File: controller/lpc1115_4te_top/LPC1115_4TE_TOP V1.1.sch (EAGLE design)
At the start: 106 parts, among them P2 ISP, Q1 BC856, Q2 BCP52, Q3 BC847C, U1 LPC1115FBD48, U2 BD9G101, U3 XO32 12MHz, X1 12MHz

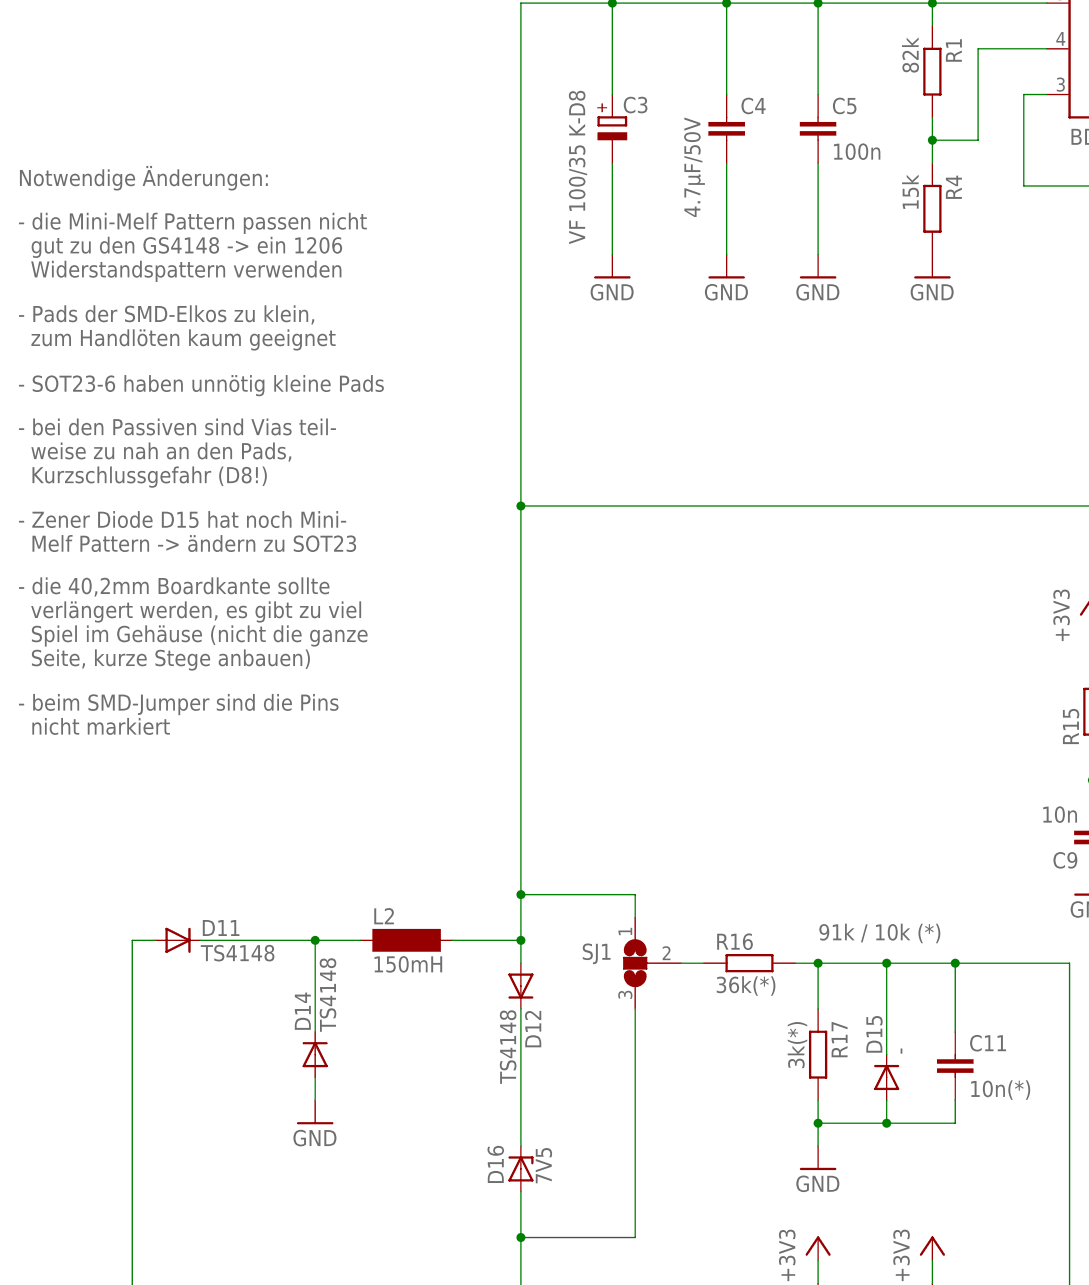
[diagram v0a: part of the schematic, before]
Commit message: Update App out6_cs, update Controller lpc1115_4te_top
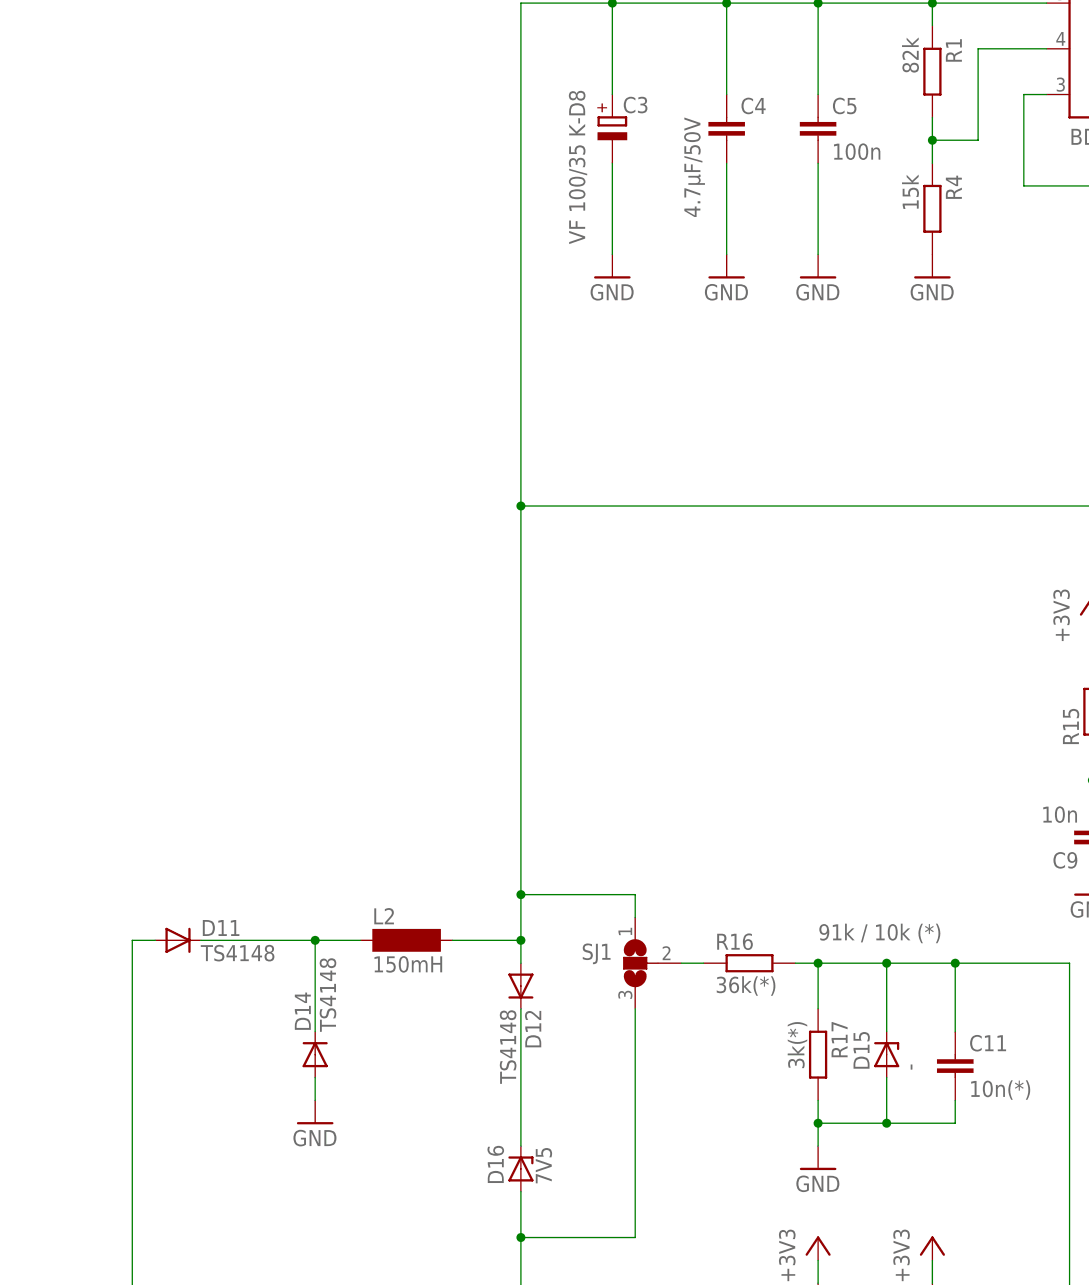
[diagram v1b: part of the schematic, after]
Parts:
- C3, C7: device rcl:CPOL-EUUD-6,3X7,7 -> rcl:CPOL-EUESMD-D
- D1, D11, D12, D14, D17, D2, D3, D4, D5, D6, D7, D8: device diode:DIODE-MINIMELF -> diode:DIODE-D0805
- D15: device diode:DIODE-MINIMELF -> diode:ZENER-DIODESOT23
- U2: device Stefan_selfbus:BD9G101GBD9G101G-SOT23-6 -> Stefan_selfbus:BD9G101GBD9G101G-SOT23-6MOD
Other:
- note removed: "- Pads der SMD-Elkos zu klein, zum Handlöten kaum geeignet"
- note removed: "- SOT23-6 haben unnötig kleine Pads"
- note removed: "- Zener Diode D15 hat noch Mini- Melf Pattern -> ändern zu SOT23"
- note removed: "- bei den Passiven sind Vias teil- weise zu nah an den Pads, Kurzschlussgefahr (D8!)"
- note removed: "- beim SMD-Jumper sind die Pins nicht markiert"
- note removed: "- die 40,2mm Boardkante sollte verlängert werden, es gibt zu viel Spiel im Gehäuse (nicht die ganze Seite, kurze Stege anbauen)"
- note removed: "- die Mini-Melf Pattern passen nicht gut zu den GS4148 -> ein 1206 Widerstandspattern verwenden"
- note removed: "Notwendige Änderungen:"
